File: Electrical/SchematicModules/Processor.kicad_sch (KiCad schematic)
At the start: 30 parts, among them J1 3220-14-0300-00, SW1 DS04-254-2L-01BK, SW2 TS04-66-65-BK-160-SMT, SW3 TS04-66-65-BK-160-SMT, SW4 TS04-66-65-BK-160-SMT, SW5 TS04-66-65-BK-160-SMT, SW6 TS04-66-65-BK-160-SMT, SW7 TS04-66-65-BK-160-SMT, U1 STM32F103T6Ux, Y1 16 MHz

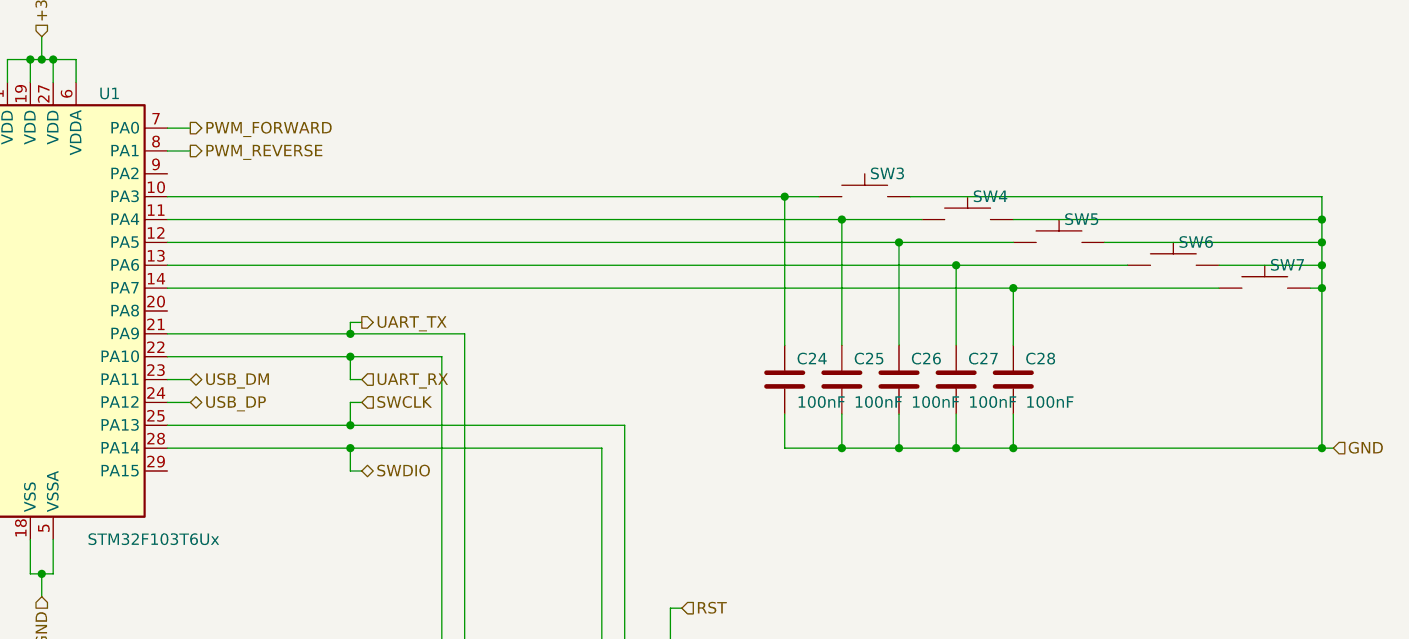
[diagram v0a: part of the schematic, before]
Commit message: Added layout for prototype 1
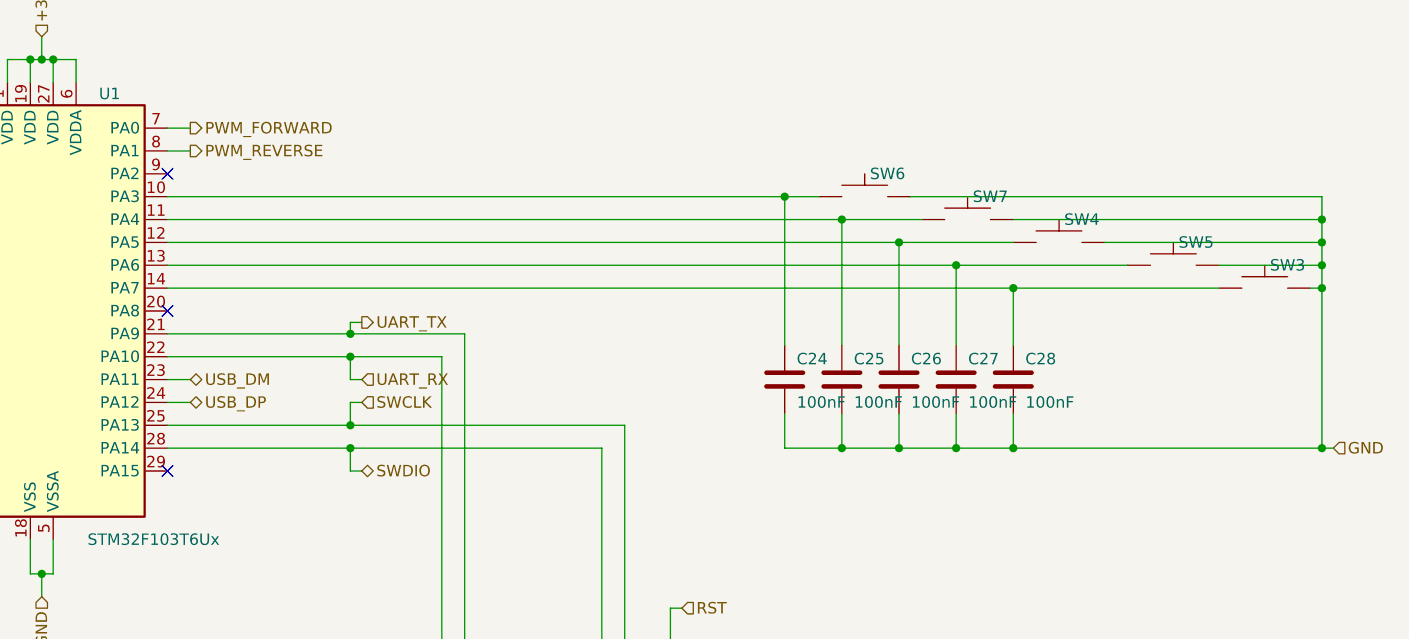
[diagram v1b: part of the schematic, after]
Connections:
- net at C27.1, U1.13 (PA6): now also SW5.1; no longer SW6.1
- net at C25.1, U1.11 (PA4): now also SW7.1; no longer SW4.1
- net at C26.1, U1.12 (PA5): now also SW4.1; no longer SW5.1
- net at C28.1, U1.14 (PA7): now also SW3.1; no longer SW7.1
- net at C24.1, U1.10 (PA3): now also SW6.1; no longer SW3.1
- no-connect marks 3 -> 6
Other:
- moved on the sheet: SW3, SW4, SW5, SW6, SW7
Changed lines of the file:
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@@
 	)
 	(no_connect
+		(at 144.78 72.39)
+	)
+	(no_connect
+		(at 144.78 87.63)
+	)
+	(no_connect
+		(at 144.78 105.41)
+	)
+	(no_connect
 		(at 187.96 125.73)
 	)
@@
 	(symbol
 		(lib_id "NyaCentralenheten:Switch")
-		(at 233.68 77.47 0)
+		(at 243.84 80.01 0)
 		(unit 1)
 		(exclude_from_sim no)
@@
 		(dnp no)
 		(property "Reference" "SW4"
-			(at 236.22 74.93 0)
+			(at 246.38 77.47 0)
 			(effects
 				(font
@@
 		)
 		(property "Value" "TS04-66-65-BK-160-SMT"
-			(at 233.68 80.01 0)
+			(at 243.84 82.55 0)
 			(effects
 				(font
@@
 		)
 		(property "Footprint" "AutoTiller:TS04-66-65-BK-160-SMT"
-			(at 233.68 77.47 0)
+			(at 243.84 80.01 0)
 			(effects
 				(font
@@
 		)
 		(property "Datasheet" "https://www.cuidevices.com/product/resource/ts04.pdf"
-			(at 233.68 77.47 0)
+			(at 243.84 80.01 0)
 			(effects
 				(font
@@
 		)
 		(property "Description" ""
-			(at 233.68 77.47 0)
+			(at 243.84 80.01 0)
 			(effects
 				(font
@@
 	(symbol
 		(lib_id "NyaCentralenheten:Switch")
-		(at 256.54 82.55 0)
+		(at 222.25 74.93 0)
 		(unit 1)
 		(exclude_from_sim no)
@@
 		(dnp no)
 		(property "Reference" "SW6"
-			(at 259.08 80.01 0)
+			(at 224.79 72.39 0)
 			(effects
 				(font
@@
 		)
 		(property "Value" "TS04-66-65-BK-160-SMT"
-			(at 256.54 85.09 0)
+			(at 222.25 77.47 0)
 			(effects
 				(font
@@
 		)
 		(property "Footprint" "AutoTiller:TS04-66-65-BK-160-SMT"
-			(at 256.54 82.55 0)
+			(at 222.25 74.93 0)
 			(effects
 				(font
@@
 		)
 		(property "Datasheet" "https://www.cuidevices.com/product/resource/ts04.pdf"
-			(at 256.54 82.55 0)
+			(at 222.25 74.93 0)
 			(effects
 				(font
@@
 		)
 		(property "Description" ""
-			(at 256.54 82.55 0)
+			(at 222.25 74.93 0)
 			(effects
 				(font
@@
 	(symbol
 		(lib_id "NyaCentralenheten:Switch")
-		(at 243.84 80.01 0)
+		(at 256.54 82.55 0)
 		(unit 1)
 		(exclude_from_sim no)
@@
 		(dnp no)
 		(property "Reference" "SW5"
-			(at 246.38 77.47 0)
+			(at 259.08 80.01 0)
 			(effects
 				(font
@@
 		)
 		(property "Value" "TS04-66-65-BK-160-SMT"
-			(at 243.84 82.55 0)
+			(at 256.54 85.09 0)
 			(effects
 				(font
@@
 		)
 		(property "Footprint" "AutoTiller:TS04-66-65-BK-160-SMT"
-			(at 243.84 80.01 0)
+			(at 256.54 82.55 0)
 			(effects
 				(font
@@
 		)
 		(property "Datasheet" "https://www.cuidevices.com/product/resource/ts04.pdf"
-			(at 243.84 80.01 0)
+			(at 256.54 82.55 0)
 			(effects
 				(font
@@
 		)
 		(property "Description" ""
-			(at 243.84 80.01 0)
+			(at 256.54 82.55 0)
 			(effects
 				(font
@@
 	(symbol
 		(lib_id "NyaCentralenheten:Switch")
-		(at 266.7 85.09 0)
+		(at 233.68 77.47 0)
 		(unit 1)
 		(exclude_from_sim no)
@@
 		(dnp no)
 		(property "Reference" "SW7"
-			(at 269.24 82.55 0)
+			(at 236.22 74.93 0)
 			(effects
 				(font
@@
 		)
 		(property "Value" "TS04-66-65-BK-160-SMT"
-			(at 266.7 87.63 0)
+			(at 233.68 80.01 0)
 			(effects
 				(font
@@
 		)
 		(property "Footprint" "AutoTiller:TS04-66-65-BK-160-SMT"
-			(at 266.7 85.09 0)
+			(at 233.68 77.47 0)
 			(effects
 				(font
@@
 		)
 		(property "Datasheet" "https://www.cuidevices.com/product/resource/ts04.pdf"
-			(at 266.7 85.09 0)
+			(at 233.68 77.47 0)
 			(effects
 				(font
@@
 		)
 		(property "Description" ""
-			(at 266.7 85.09 0)
+			(at 233.68 77.47 0)
 			(effects
 				(font
@@
 	(symbol
 		(lib_id "NyaCentralenheten:Switch")
-		(at 222.25 74.93 0)
+		(at 266.7 85.09 0)
 		(unit 1)
 		(exclude_from_sim no)
@@
 		(dnp no)
 		(property "Reference" "SW3"
-			(at 224.79 72.39 0)
+			(at 269.24 82.55 0)
 			(effects
 				(font
@@
 		)
 		(property "Value" "TS04-66-65-BK-160-SMT"
-			(at 222.25 77.47 0)
+			(at 266.7 87.63 0)
 			(effects
 				(font
@@
 		)
 		(property "Footprint" "AutoTiller:TS04-66-65-BK-160-SMT"
-			(at 222.25 74.93 0)
+			(at 266.7 85.09 0)
 			(effects
 				(font
@@
 		)
 		(property "Datasheet" "https://www.cuidevices.com/product/resource/ts04.pdf"
-			(at 222.25 74.93 0)
+			(at 266.7 85.09 0)
 			(effects
 				(font
@@
 		)
 		(property "Description" ""
-			(at 222.25 74.93 0)
+			(at 266.7 85.09 0)
 			(effects
 				(font

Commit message: Finalizing the layout
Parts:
- C28: now not fitted
- SW3: value TS04-66-65-BK-160-SMT -> TS04-66-95-BK-260-SMT; now not fitted
- SW4, SW5, SW6, SW7: value TS04-66-65-BK-160-SMT -> TS04-66-95-BK-260-SMT
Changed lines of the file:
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@@
 			)
 		)
-		(property "Value" "TS04-66-65-BK-160-SMT"
+		(property "Value" "TS04-66-95-BK-260-SMT"
 			(at 243.84 82.55 0)
 			(effects
@@
 			)
 		)
-		(property "Value" "TS04-66-65-BK-160-SMT"
+		(property "Value" "TS04-66-95-BK-260-SMT"
 			(at 222.25 77.47 0)
 			(effects
@@
 			)
 		)
-		(property "Value" "TS04-66-65-BK-160-SMT"
+		(property "Value" "TS04-66-95-BK-260-SMT"
 			(at 256.54 85.09 0)
 			(effects
@@
 			)
 		)
-		(property "Value" "TS04-66-65-BK-160-SMT"
+		(property "Value" "TS04-66-95-BK-260-SMT"
 			(at 233.68 80.01 0)
 			(effects
@@
 		(exclude_from_sim no)
 		(in_bom yes)
-		(on_board yes)
-		(dnp no)
+		(on_board no)
+		(dnp yes)
 		(property "Reference" "SW3"
 			(at 269.24 82.55 0)
@@
 			)
 		)
-		(property "Value" "TS04-66-65-BK-160-SMT"
+		(property "Value" "TS04-66-95-BK-260-SMT"
 			(at 266.7 87.63 0)
 			(effects
@@
 		(in_bom yes)
 		(on_board yes)
-		(dnp no)
+		(dnp yes)
 		(property "Reference" "C28"
 			(at 241.808 92.964 0)
